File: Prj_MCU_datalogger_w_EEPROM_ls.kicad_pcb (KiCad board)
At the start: 2 copper layers, 29 parts, among them J1 Conn_01x04_Pin, J2 Conn_01x04_Pin, J3 Conn_01x09_Pin, J4 Conn_02x03_Odd_Even, U1 24LC1025, U2 24LC1025, U3 ATMEGA328P-AU, U4 DS1337S_, Y1 16 MHz, Y2 32.768 kHz

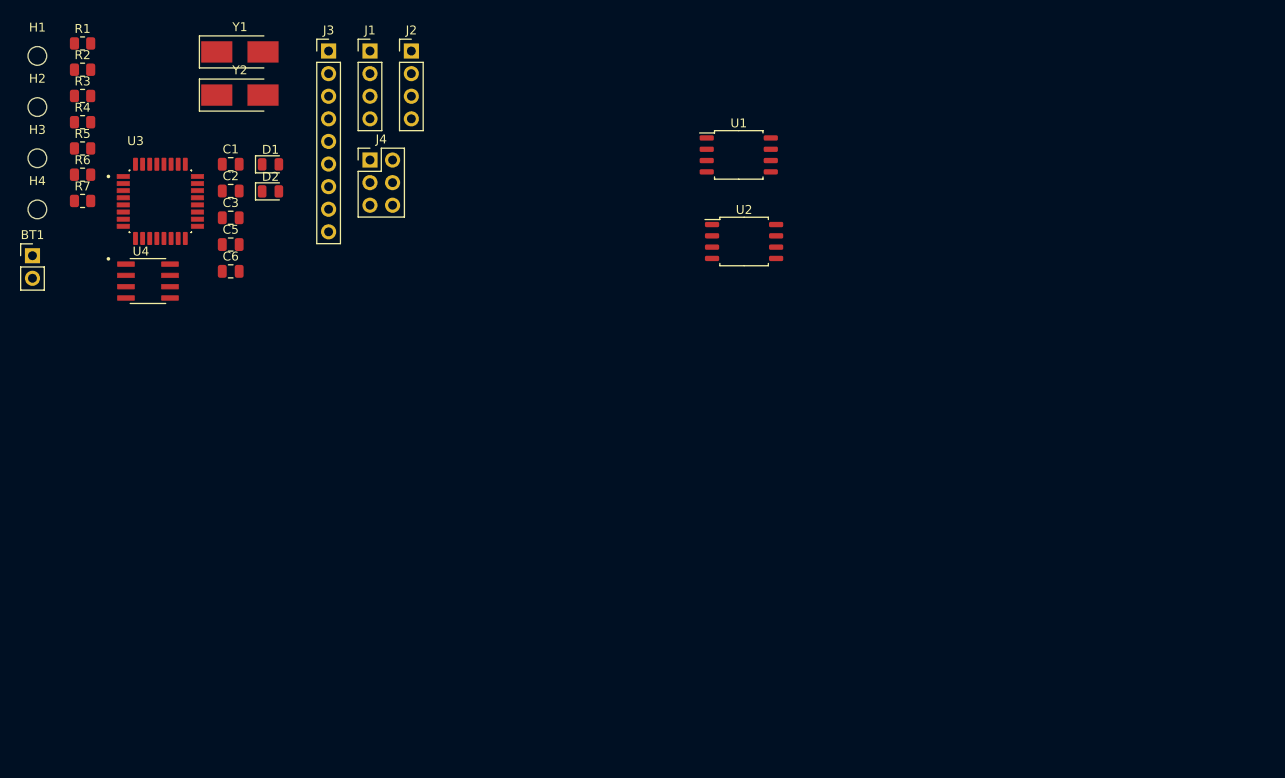
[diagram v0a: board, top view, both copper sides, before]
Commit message: Completed placement of footprints
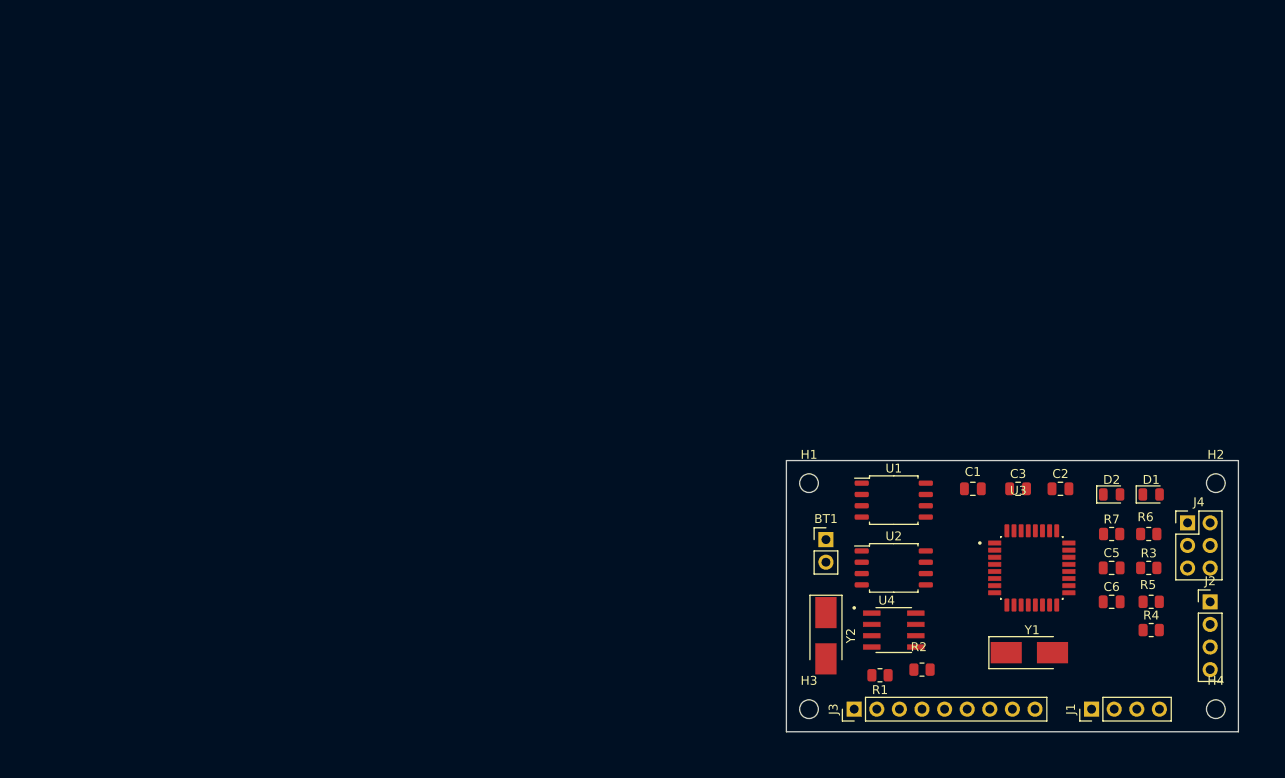
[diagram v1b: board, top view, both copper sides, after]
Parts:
- moved H4 143.9 mm to (269.2, 154.9)
- moved H2 139.0 mm to (269.2, 129.5)
- moved R4 133.0 mm to (262.0, 146.1)
- moved R3 131.0 mm to (261.7, 139.1)
- moved R5 130.5 mm to (262.0, 142.9)
- moved R6 126.4 mm to (261.7, 135.3)
- moved R7 121.6 mm to (257.5, 135.3)
- moved R2 116.0 mm to (236.2, 150.5)
- moved R1 114.3 mm to (231.5, 151.1), turned to 180 degrees
- moved Y1 111.5 mm to (248.3, 148.6)
- moved J1 109.8 mm to (255.3, 154.9), turned to 90 degrees
- moved J2 109.0 mm to (268.6, 142.9)
- moved H3 106.6 mm to (223.5, 154.9)
- moved U3 106.2 mm to (248.6, 139.1)
- moved C6 105.7 mm to (257.5, 142.9)
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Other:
- board outline added: 50.8 x 30.5 mm

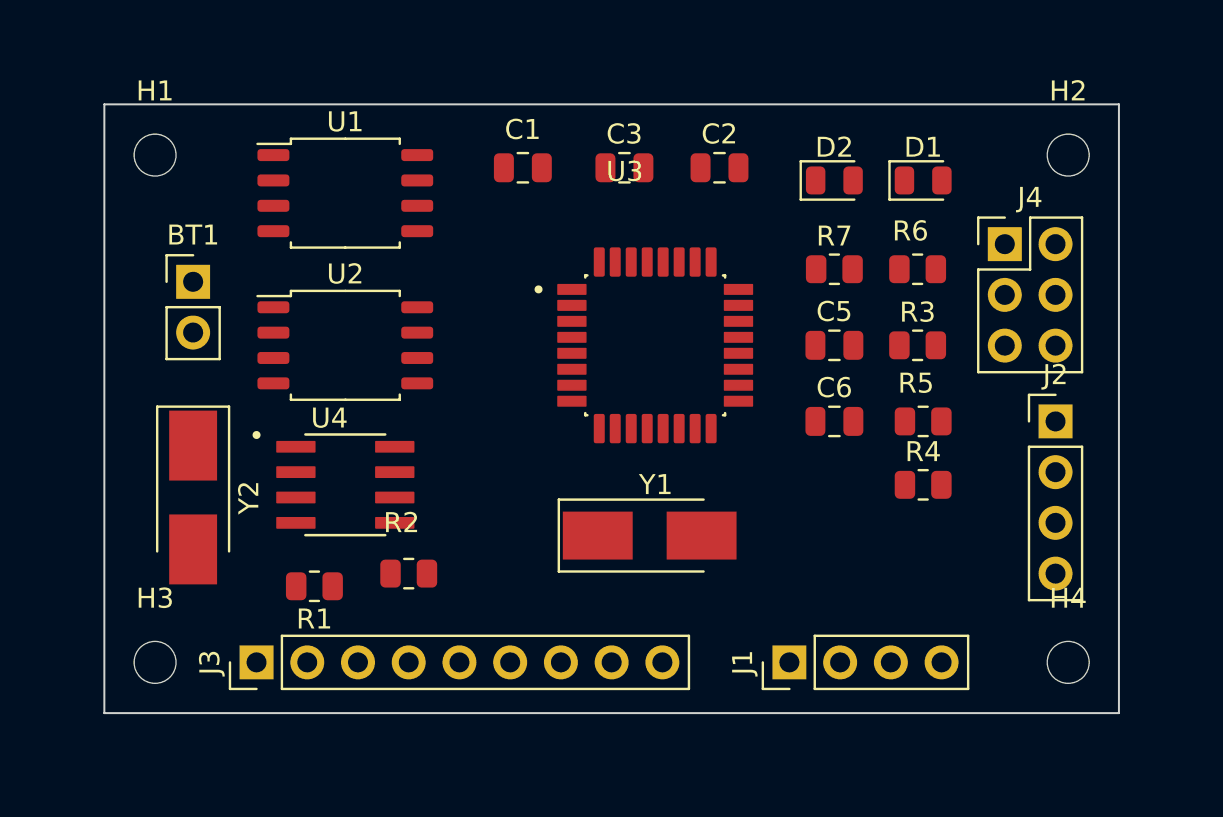
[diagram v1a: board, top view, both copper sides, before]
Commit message: Routing sans GND completed
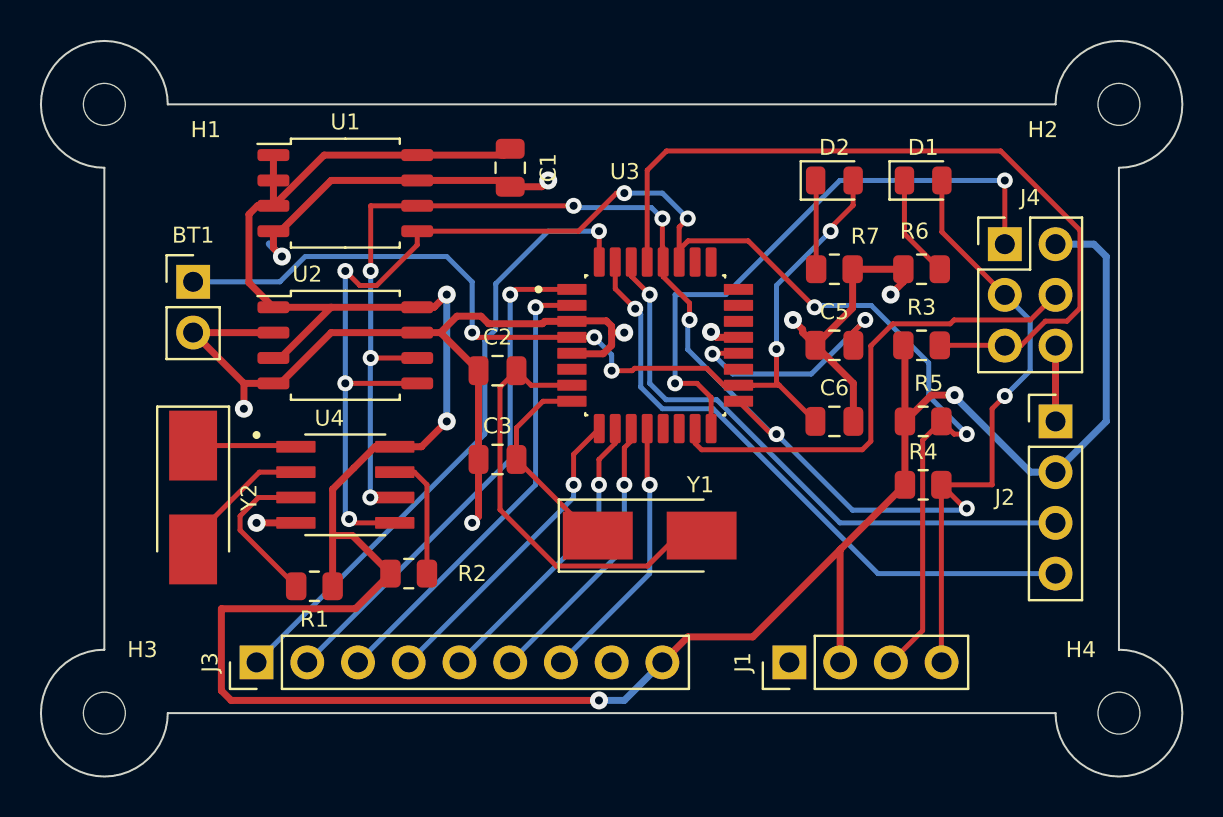
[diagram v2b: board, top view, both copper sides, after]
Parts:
- moved C3 15.9 mm to (240.7, 144.8)
- moved C2 15.1 mm to (240.7, 140.3)
- moved H1 3.59 mm to (221.0, 127.0)
- moved H3 3.59 mm to (221.0, 157.5)
- moved H2 3.59 mm to (271.8, 127.0)
- moved H4 3.59 mm to (271.8, 157.5)
- moved C1 0.63 mm to (241.3, 130.2), turned to -90 degrees
- moved R3 0.20 mm to (261.9, 139.1)
- moved R6 0.20 mm to (261.9, 135.3)
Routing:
- net /Vcc: track 0.00 -> 146.3 mm, vias 0 -> 4
- net /SCK: track 0.00 -> 92.0 mm, vias 0 -> 9
- net GND: track 0.00 -> 82.9 mm, vias 0 -> 9
- net /SDA: track 0.00 -> 76.4 mm, vias 0 -> 7
- net Net-(BT1-+): track 0.00 -> 50.0 mm, vias 0 -> 5
- net /RESET: track 0.00 -> 40.0 mm
- net /D2: track 0.00 -> 31.7 mm, vias 0 -> 1
- net /TX: track 0.00 -> 31.4 mm, vias 0 -> 1
- net /MISO: track 0.00 -> 30.2 mm, vias 0 -> 2
- net /RX: track 0.00 -> 29.7 mm, vias 0 -> 1
- net /D3: track 0.00 -> 25.8 mm, vias 0 -> 1
- net /MOSI: track 0.00 -> 24.9 mm
- net /D4: track 0.00 -> 23.3 mm, vias 0 -> 1
- net Net-(U3-PB6): track 0.00 -> 22.3 mm
- net /D5: track 0.00 -> 15.7 mm, vias 0 -> 1
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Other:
- board size 50.8 x 30.5 mm -> 57.1 x 36.8 mm

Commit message: Completed routing
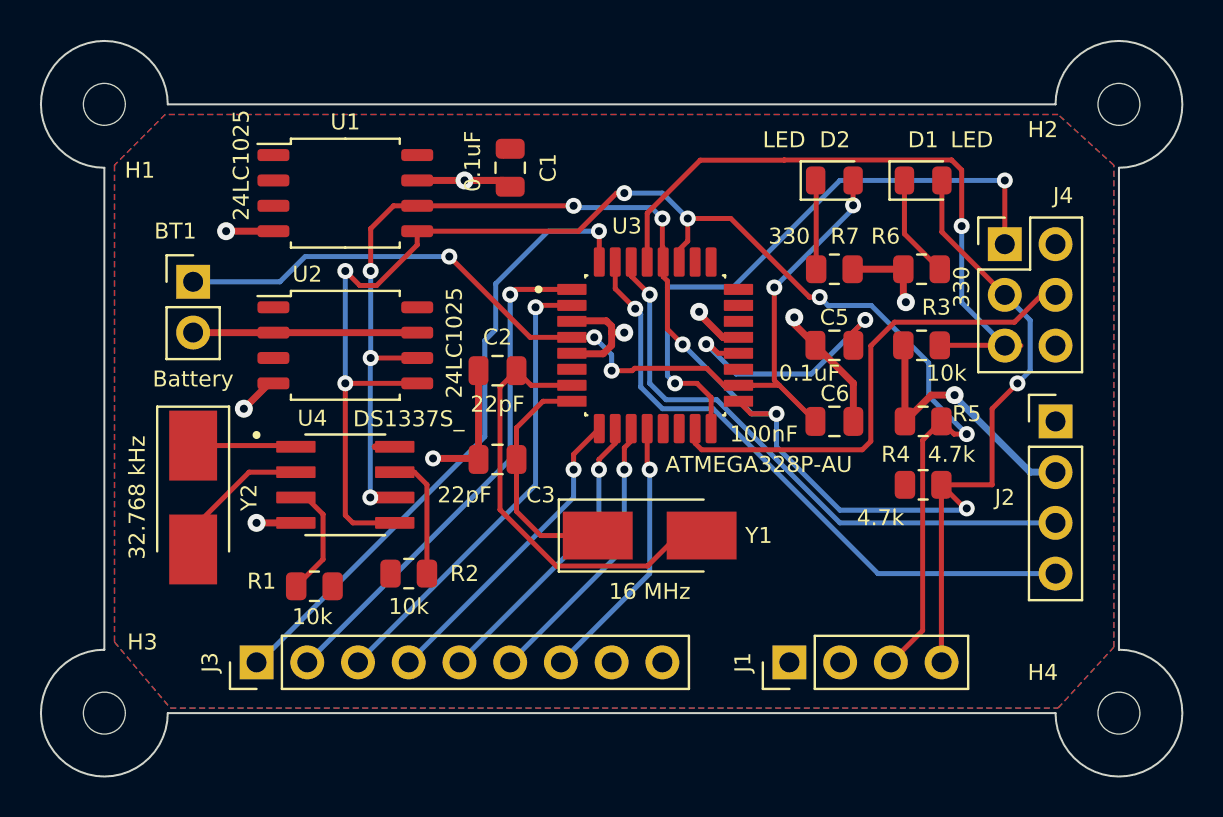
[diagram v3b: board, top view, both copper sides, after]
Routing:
- net /Vcc: track 146.3 -> 15.3 mm, vias 4 -> 1
- net GND: track 82.9 -> 50.9 mm
- net /RESET: track 40.0 -> 33.3 mm, vias 0 -> 1
- net Net-(U4-~{INTA}): track 7.86 -> 5.87 mm
- net Net-(BT1-+): track 50.0 -> 48.4 mm
- net Net-(U3-PB7): track 10.6 -> 12.1 mm
- net /SDA: track 76.4 -> 75.2 mm, vias 7 -> 6
- net /MISO: track 30.2 -> 30.9 mm
- net Net-(U3-AREF): track 12.4 -> 13.0 mm
- added copper zone on F.Cu, net /Vcc
- added copper zone on B.Cu, net GND

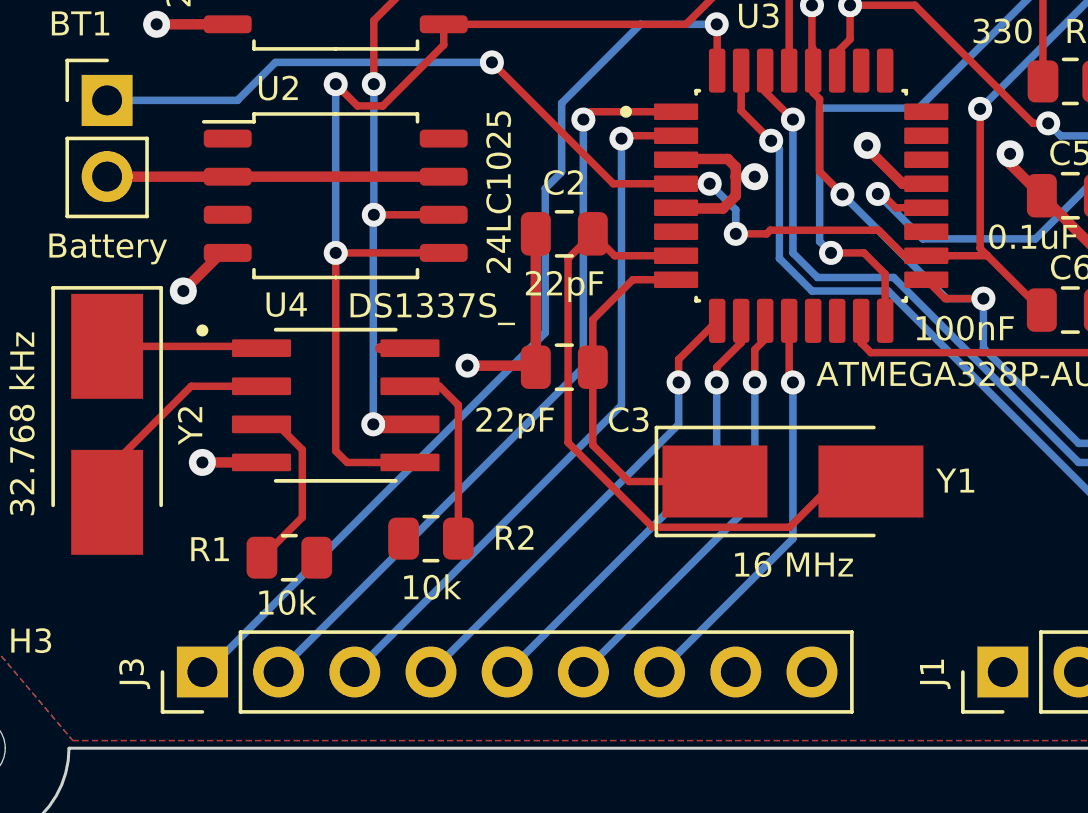
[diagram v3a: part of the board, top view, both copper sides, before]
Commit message: Refined routing
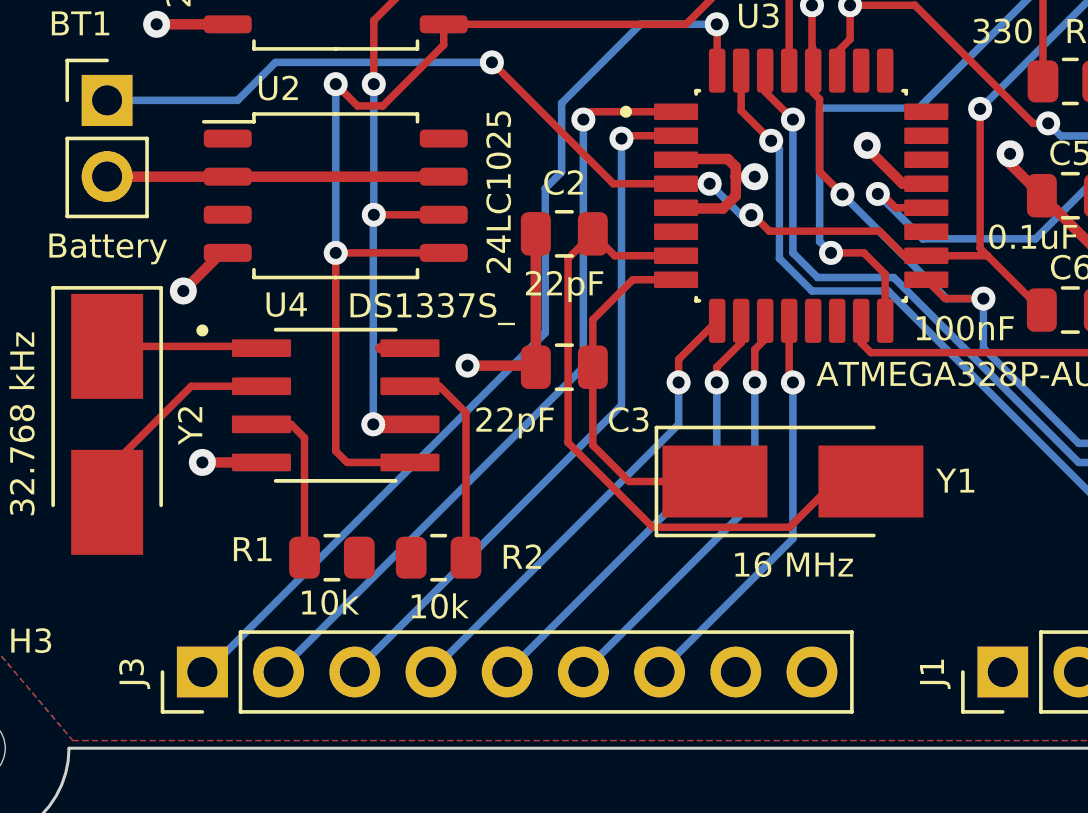
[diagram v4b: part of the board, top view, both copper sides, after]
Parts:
- moved R1 1.42 mm to (232.9, 151.1)
- moved R2 0.68 mm to (236.5, 151.1)
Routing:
- net Net-(U4-SQW/~INT): track 6.32 -> 7.07 mm
- net Net-(BT1-+): track 48.4 -> 47.8 mm
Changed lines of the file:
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@@
   )
   (footprint "Resistor_SMD:R_0805_2012Metric" (layer "F.Cu")
-    (at 236.22 150.495)
+    (at 236.474 151.13)
     (descr "Resistor SMD 0805 (2012 Metric), square (rectangular) end terminal, IPC_7351 nominal, (Body size source: IPC-SM-782 page 72, https://www.pcb-3d.com/wordpress/wp-content/uploads/ipc-sm-782a_amendment_1_and_2.pdf), generated with kicad-footprint-generator")
     (tags "resistor")
@@
   )
   (footprint "Resistor_SMD:R_0805_2012Metric" (layer "F.Cu")
-    (at 231.4975 151.13 180)
+    (at 232.918 151.13 180)
     (descr "Resistor SMD 0805 (2012 Metric), square (rectangular) end terminal, IPC_7351 nominal, (Body size source: IPC-SM-782 page 72, https://www.pcb-3d.com/wordpress/wp-content/uploads/ipc-sm-782a_amendment_1_and_2.pdf), generated with kicad-footprint-generator")
     (tags "resistor")
@@
   (gr_arc (start 271.78 154.305) (mid 274.025064 159.725064) (end 268.605 157.48)
     (stroke (width 0.1) (type default)) (layer "Edge.Cuts"))
-  (segment (start 251.144501 140.2145) (end 251.995001 141.065) (width 0.25) (layer "F.Cu") (net 1))
   (segment (start 238.252 134.62) (end 242.297 138.665) (width 0.25) (layer "F.Cu") (net 1))
   (segment (start 252.73 141.065) (end 254.7725 141.065) (width 0.25) (layer "F.Cu") (net 1))
-  (segment (start 247.5295 140.2145) (end 247.409 140.335) (width 0.25) (layer "F.Cu") (net 1))
+  (segment (start 251.175001 140.245) (end 251.995001 141.065) (width 0.25) (layer "F.Cu") (net 1))
+  (segment (start 246.966393 139.712393) (end 247.499 140.245) (width 0.25) (layer "F.Cu") (net 1))
+  (segment (start 251.995001 141.065) (end 252.73 141.065) (width 0.25) (layer "F.Cu") (net 1))
+  (segment (start 246.898628 139.712393) (end 246.966393 139.712393) (width 0.25) (layer "F.Cu") (net 1))
   (segment (start 254.7725 141.065) (end 256.5825 142.875) (width 0.25) (layer "F.Cu") (net 1))
-  (segment (start 247.5295 140.2145) (end 251.144501 140.2145) (width 0.25) (layer "F.Cu") (net 1))
+  (segment (start 247.499 140.245) (end 251.175001 140.245) (width 0.25) (layer "F.Cu") (net 1))
   (segment (start 254.524951 136.169549) (end 254.524951 140.817451) (width 0.25) (layer "F.Cu") (net 1))
   (segment (start 253.464999 141.065) (end 252.73 141.065) (width 0.25) (layer "F.Cu") (net 1))
@@
   (segment (start 254.524951 140.817451) (end 254.7725 141.065) (width 0.25) (layer "F.Cu") (net 1))
   (segment (start 258.47 132.055) (end 258.47 130.81) (width 0.25) (layer "F.Cu") (net 1))
-  (segment (start 247.409 140.335) (end 246.38 140.335) (width 0.25) (layer "F.Cu") (net 1))
   (segment (start 245.51 138.665) (end 244.39 138.665) (width 0.25) (layer "F.Cu") (net 1))
-  (segment (start 251.995001 141.065) (end 252.73 141.065) (width 0.25) (layer "F.Cu") (net 1))
   (via (at 254.524951 136.169549) (size 0.8) (drill 0.4) (layers "F.Cu" "B.Cu") (net 1))
   (via (at 238.252 134.62) (size 0.8) (drill 0.4) (layers "F.Cu" "B.Cu") (net 1))
   (via (at 258.47 132.055) (size 0.8) (drill 0.4) (layers "F.Cu" "B.Cu") (net 1))
   (via (at 245.51 138.665) (size 0.8) (drill 0.4) (layers "F.Cu" "B.Cu") (net 1))
-  (via (at 246.38 140.335) (size 0.8) (drill 0.4) (layers "F.Cu" "B.Cu") (net 1))
+  (via (at 246.898628 139.712393) (size 0.8) (drill 0.4) (layers "F.Cu" "B.Cu") (net 1))
+  (segment (start 246.898628 139.712393) (end 246.557393 139.712393) (width 0.25) (layer "B.Cu") (net 1))
   (segment (start 229.771727 135.885) (end 225.425 135.885) (width 0.25) (layer "B.Cu") (net 1))
-  (segment (start 246.38 140.335) (end 246.38 139.535) (width 0.25) (layer "B.Cu") (net 1))
   (segment (start 238.252 134.62) (end 231.036727 134.62) (width 0.25) (layer "B.Cu") (net 1))
   (segment (start 258.47 132.2245) (end 258.47 132.055) (width 0.25) (layer "B.Cu") (net 1))
   (segment (start 254.524951 136.169549) (end 258.47 132.2245) (width 0.25) (layer "B.Cu") (net 1))
+  (segment (start 246.557393 139.712393) (end 245.51 138.665) (width 0.25) (layer "B.Cu") (net 1))
   (segment (start 231.036727 134.62) (end 229.771727 135.885) (width 0.25) (layer "B.Cu") (net 1))
-  (segment (start 246.38 139.535) (end 245.51 138.665) (width 0.25) (layer "B.Cu") (net 1))
   (segment (start 229.792328 140.97) (end 229.445 140.97) (width 0.35) (layer "F.Cu") (net 2))
   (segment (start 239.66301 144.72801) (end 239.715 144.78) (width 0.35) (layer "F.Cu") (net 2))
@@
   (segment (start 263.906 136.921) (end 266.065 139.08) (width 0.25) (layer "B.Cu") (net 22))
   (segment (start 263.906 133.096) (end 263.906 136.921) (width 0.25) (layer "B.Cu") (net 22))
-  (segment (start 230.585 151.13) (end 231.93 149.784999) (width 0.25) (layer "F.Cu") (net 23))
-  (segment (start 231.93 149.784999) (end 231.93 147.527718) (width 0.25) (layer "F.Cu") (net 23))
-  (segment (start 231.087282 146.685) (end 230.57 146.685) (width 0.25) (layer "F.Cu") (net 23))
-  (segment (start 231.93 147.527718) (end 231.087282 146.685) (width 0.25) (layer "F.Cu") (net 23))
+  (segment (start 231.554999 146.685) (end 230.57 146.685) (width 0.25) (layer "F.Cu") (net 23))
+  (segment (start 232.0055 147.135501) (end 231.554999 146.685) (width 0.25) (layer "F.Cu") (net 23))
+  (segment (start 232.0055 151.13) (end 232.0055 147.135501) (width 0.25) (layer "F.Cu") (net 23))
+  (segment (start 236.504999 145.415) (end 237.3865 146.296501) (width 0.25) (layer "F.Cu") (net 24))
+  (segment (start 237.3865 146.296501) (end 237.3865 151.13) (width 0.25) (layer "F.Cu") (net 24))
   (segment (start 235.52 145.415) (end 236.504999 145.415) (width 0.25) (layer "F.Cu") (net 24))
-  (segment (start 236.504999 145.415) (end 237.1325 146.042501) (width 0.25) (layer "F.Cu") (net 24))
-  (segment (start 237.1325 146.042501) (end 237.1325 150.495) (width 0.25) (layer "F.Cu") (net 24))
   (segment (start 230.51 144.085) (end 230.57 144.145) (width 0.25) (layer "F.Cu") (net 34))
   (segment (start 225.425 144.085) (end 230.51 144.085) (width 0.25) (layer "F.Cu") (net 34))

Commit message: Refined routing.v2
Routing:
- net GND: track 50.9 -> 49.9 mm
